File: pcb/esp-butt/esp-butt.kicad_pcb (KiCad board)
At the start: 2 copper layers, 65 x 65 mm, 20 parts, among them J1 1x04_P2.54mm, J2 JST_XH_B2B, U1 XIAO-ESP32-C3

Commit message: More stuffs
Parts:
- J2: value JST_XH_B2B -> JST_PH; footprint Connector_JST:JST_XH_B2B-XH-A_1x02_P2.50mm_Vertical -> Connector_JST:JST_PH_B2B-PH-K_1x02_P2.00mm_Vertical
- R10, R9: moved to B.Cu
- moved R10 19.1 mm to (76.2, 68.0), turned to -90 degrees
- moved J2 17.4 mm to (86.5, 87.2)
- moved R9 1.59 mm to (79.2, 78.2), turned to 90 degrees
- moved R1 1.13 mm to (77.5, 114.7)
- moved R5 1.13 mm to (101.5, 114.7)
- moved R6 1.13 mm to (104.5, 114.7)
- moved C1 1.13 mm to (83.5, 100.3)
- moved C2 1.13 mm to (80.5, 100.3)
- moved C3 1.13 mm to (100.2, 100.3), turned to 0 degrees
- moved R2 1.13 mm to (83.5, 104.5)
- moved R3 1.13 mm to (74.5, 104.5)
- moved R4 1.13 mm to (80.5, 104.5)
- moved S1 1.13 mm to (92.5, 110.0)
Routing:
- net /BAT-: track 20.7 -> 37.6 mm
- net /BAT+: track 16.8 -> 33.2 mm
- net /A2: track 26.0 -> 10.0 mm
- net /SCL: track 22.6 -> 26.6 mm
- net /SDA: track 24.7 -> 27.9 mm
- net +3.3V: track 155.5 -> 157.3 mm
- net /DT: track 50.2 -> 51.2 mm
- net /CLK: track 45.2 -> 46.2 mm
- net /SW: track 45.7 -> 45.2 mm
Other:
- outline, holes or cut-outs redrawn

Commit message: workies
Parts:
- removed H1, H2: MountingHole, MountingHole:MountingHole_2.2mm_M2
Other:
- board text added: "esp-butt Rev: 0.2"

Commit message: More work + docs
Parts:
- moved R1 40.4 mm to (55.8, 80.6)
- moved R5 40.4 mm to (79.8, 80.6)
- moved R6 40.4 mm to (82.8, 80.6)
- moved U1 40.4 mm to (72.1, 36.4)
- moved C1 40.4 mm to (61.8, 66.2)
- moved C2 40.4 mm to (58.8, 66.2)
- moved C3 40.4 mm to (78.5, 66.2)
- moved J1 40.4 mm to (70.8, 59.9)
- moved J2 40.4 mm to (64.8, 53.1)
- moved R10 40.4 mm to (54.5, 33.9)
- moved R2 40.4 mm to (61.8, 70.4)
- moved R3 40.4 mm to (52.8, 70.4)
- moved R4 40.4 mm to (58.8, 70.4)
- moved R7 40.4 mm to (45.2, 58.4)
- moved R8 40.4 mm to (96.2, 58.4)
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
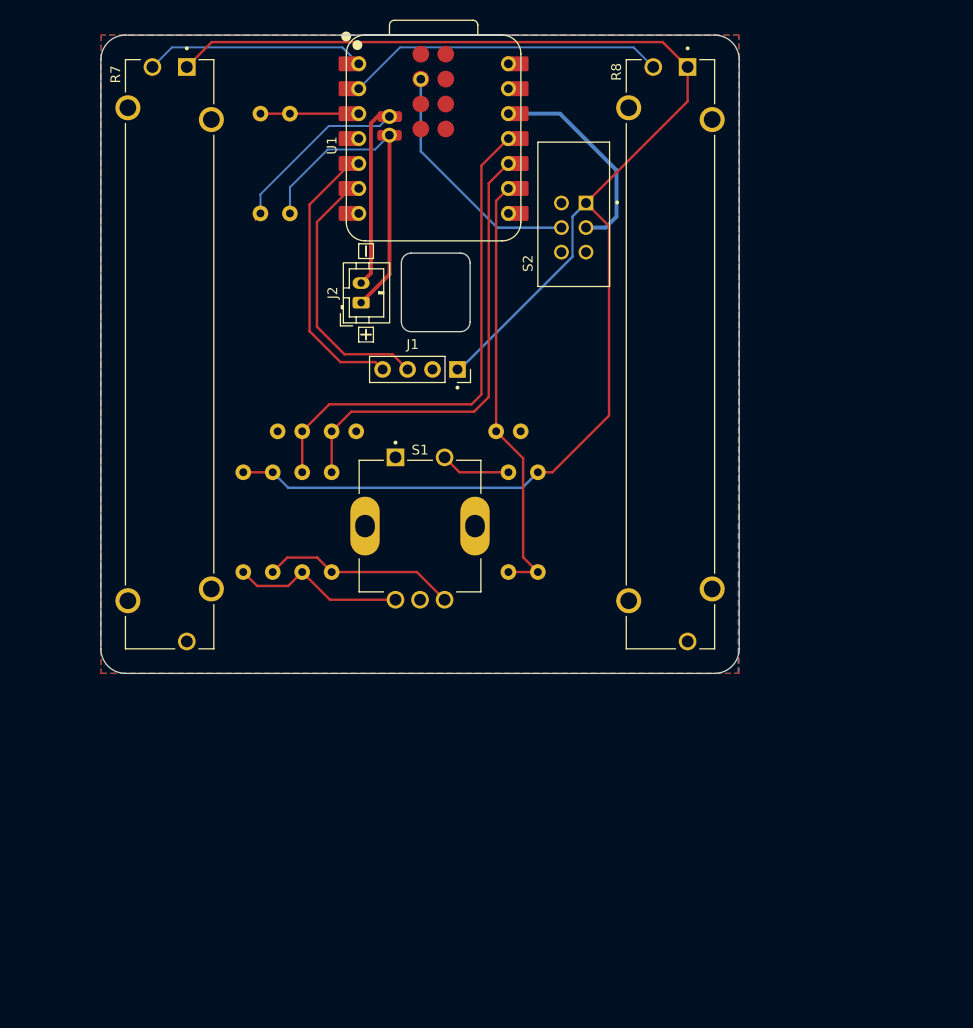
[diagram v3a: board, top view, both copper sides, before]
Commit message: Add Pillow dependency and implement session recording feature
- Added "pillow" to dependencies in pyproject.toml and uv.lock.
- Enhanced HardwareMock to support session recording, including:
  - New spawn_recorder_task function to handle event and frame recording.
  - Logic to create a temporary directory for storing frames.
  - Recording navigation and slider events to a specified NDJSON file.
  - Saving frames as PNG images during the session.
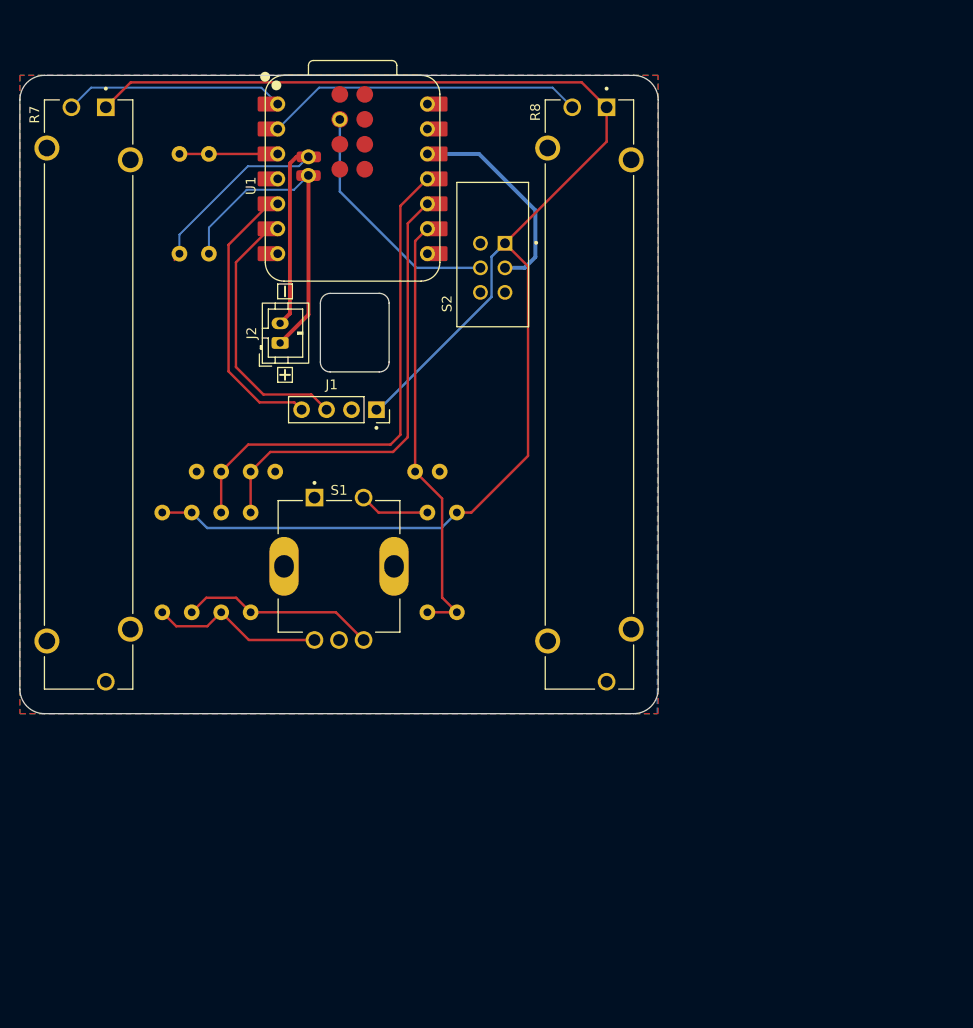
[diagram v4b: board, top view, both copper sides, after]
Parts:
- moved R1 9.21 mm to (47.5, 84.7)
- moved R5 9.21 mm to (71.5, 84.7)
- moved R6 9.21 mm to (74.5, 84.7)
- moved J1 9.21 mm to (62.5, 64.0)
- moved J2 9.21 mm to (56.5, 57.2)
- moved R10 9.21 mm to (46.2, 38.0)
- moved R7 9.21 mm to (37.0, 62.5)
- moved R8 9.21 mm to (88.0, 62.5)
- moved S2 9.21 mm to (79.4, 47.1)
- moved C1 9.21 mm to (53.5, 70.3)
- moved C2 9.21 mm to (50.5, 70.3)
- moved C3 9.21 mm to (70.2, 70.3)
- moved R2 9.21 mm to (53.5, 74.5)
- moved R3 9.21 mm to (44.5, 74.5)
- moved R4 9.21 mm to (50.5, 74.5)
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
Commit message: Documentation updates
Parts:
- U1: value XIAO-ESP32-C3 -> XIAO-ESP32-S3
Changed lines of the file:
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@@
 			)
 		)
-		(property "Value" "XIAO-ESP32-C3"
+		(property "Value" "XIAO-ESP32-S3"
 			(at 0 0 90)
 			(unlocked yes)
